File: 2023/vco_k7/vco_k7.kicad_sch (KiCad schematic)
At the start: 23 parts, among them M1 PMOS_OR1, M10 NMOS_OR1, M11 NMOS_OR1, M12 PMOS_OR1, M13 PMOS_OR1, M14 NMOS_OR1, M15 NMOS_OR1, M16 PMOS_OR1, M17 PMOS_OR1, M18 NMOS_OR1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

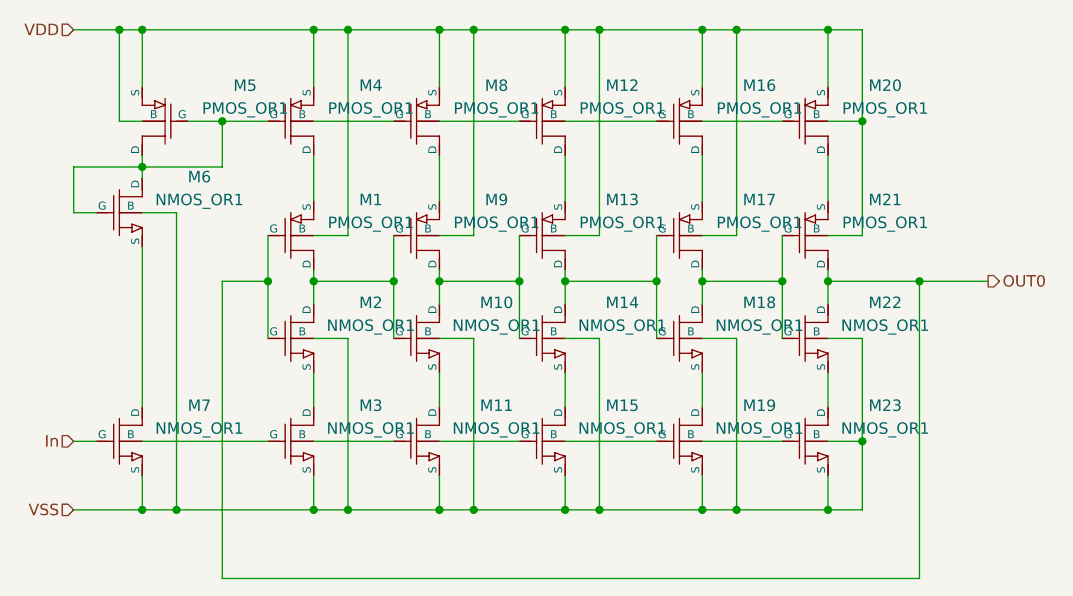
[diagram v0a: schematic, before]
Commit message: VCO 回路図を見直してちゃんとシミュレーションできるようにした。
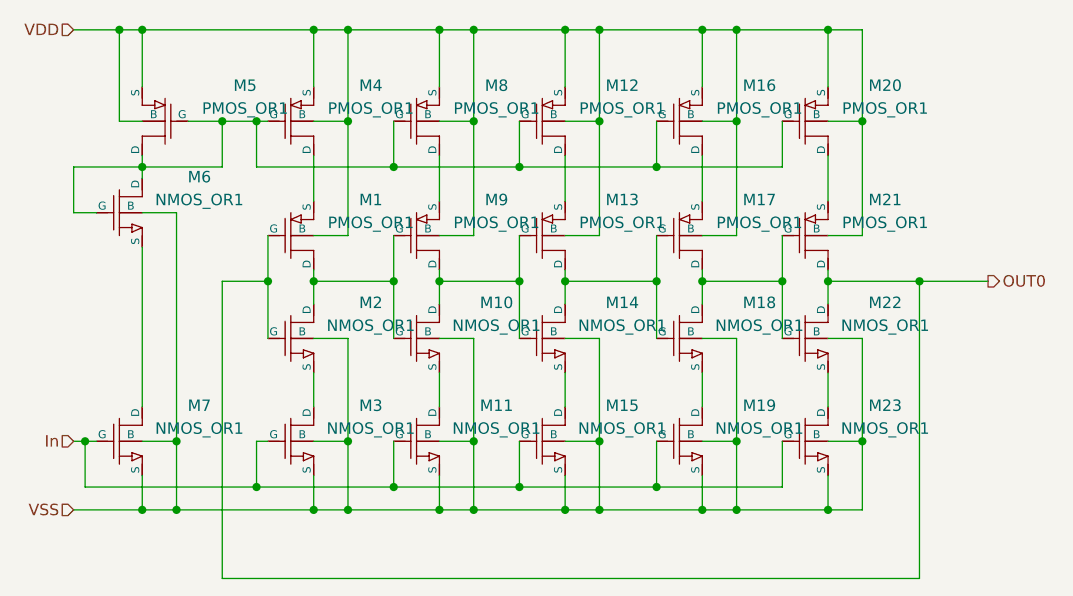
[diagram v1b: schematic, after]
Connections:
- net In: now also M11.2 (G), M15.2 (G), M19.2 (G), M23.2 (G), M3.2 (G)
- net VDD: now also M12.4 (B), M16.4 (B), M4.4 (B), M8.4 (B)
- net VSS: now also M11.4 (B), M15.4 (B), M19.4 (B), M3.4 (B), M7.4 (B)
- net at M12.2 (G): now also M16.2 (G), M20.2 (G), M4.2 (G), M5.1 (D), M5.2 (G), M6.1 (D), M6.2 (G), M8.2 (G); no longer M8.4 (B)
